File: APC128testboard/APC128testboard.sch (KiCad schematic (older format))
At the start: 75 parts, among them P1 MAXV_CONNB, P10 SPYPAD, P11 SPYPAD, P12 SPYPAD, P13 SPYPAD, P14 SPYPAD, P15 SPYPAD, P16 SPYPAD, P17 SPYPAD, P18 BNC, P19 SPYPAD, P2 MAXV_CONNA, P20 SPYPAD, P21 SPYPAD, P22 SPYPAD, P23 SPYPAD, P24 SPYPAD, P25 SPYPAD, P26 SPYPAD, P3 SPYPAD, P4 SPYPAD, P5 SPYPAD, P6 SPYPAD, P7 SPYPAD, P8 SPYPAD, P9 SPYPAD, SW1 SWITCH_INV, SW2 SWITCH_INV, SW3 SWITCH_INV, SW4 SWITCH_INV, SW5 SWITCH_INV, U1 APC128, U2 AD8129, U3 AD8129, U4 AD5334

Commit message: single library integrated into project settings.
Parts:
- removed P18: BNC, symbol BNC
- removed SW1, SW2, SW3, SW4: SWITCH_INV, symbol SWITCH_INV
- added JP? (x4): JUMPER3, symbol JUMPER3
- added P?: AMP_PWR, symbol CONN_2
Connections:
- wire segments 182 -> 215
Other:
- note removed: "To Oscilloscope"
- moved on the sheet: P20, P21, P22, P23

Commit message: Update to second proposed design of APC128Testboard
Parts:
- removed P1: MAXV_CONNB, symbol CONN_20X2
- removed P?: AMP_PWR, symbol CONN_2
- removed R10, R12, R14, R16, R18, R20, R22, R24, R26, R28: 300, symbol R
- removed R11, R13, R15, R17, R19, R21, R23, R25, R27: 43, symbol R
- removed R29, R30, R31, R32: R, symbol R
- removed SW5: SWITCH_INV, symbol SWITCH_INV
- added C6, C7: 1uF, symbol C
- added C? (x4): .1uF, symbol C
- added C? (x4): 10uF, symbol C
- added JP1, JP2, JP7: JUMPER3, symbol JUMPER3
- added K1: AMP_PWR, symbol CONN_3
- added K2: LEMO+, symbol LEMO2
- added K3: LEMO-, symbol LEMO2
- added P1, P18, P27, P28, P29, P30: SPYPAD, symbol SPYPAD
- added RP1, RP3: 43, symbol R_PACK8
- added RP2, RP4: 300, symbol R_PACK8
- added U5: MAX1719, MODULE, symbol MAX1719
- R1: value 43 -> RG
- R2: value 300 -> RF
- R3: value 43 -> 50
- R4: value 300 -> RG
- R5: value 43 -> RF
- R6: value 300 -> 50
- R7: value 43 -> R
- R8: value 300 -> 0
- R9: value 43 -> 0
- gave numbers to parts that had none: 4
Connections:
- net labels added: -5V, Out+, Out-, Vamp+, Vamp-
- wire segments 215 -> 232
- no-connect marks 5 -> 19
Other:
- note added: "-5V Voltage Regulator"
- note added: "Amp Voltage Source Selector"
- note added: "Fast amplifiers"
- note added: "POTs for setting some \nanalog levels"
- note added: "Select Pot or DAC as \nanalog sources for APC"
- note added: "To scope"
- note removed: "Fast amplifiers. Not sure if this is correct configuration."
- note removed: "Select Pot or DAC as \nanalog source"
- moved on the sheet: C1, JP3, JP4, JP5, JP6, P17, R33, R34, RV3, RV4, U1, U2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

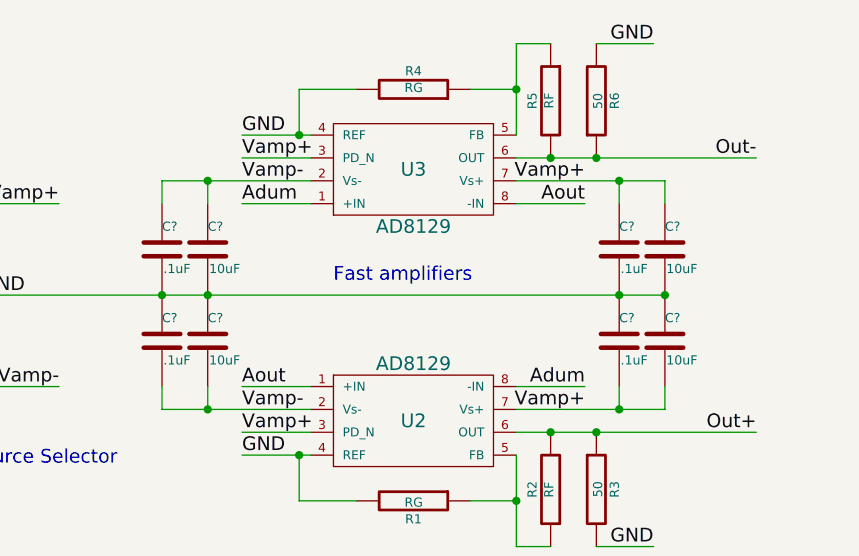
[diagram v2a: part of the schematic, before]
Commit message: Annotated parts on schematic.
Created some missing footprints.
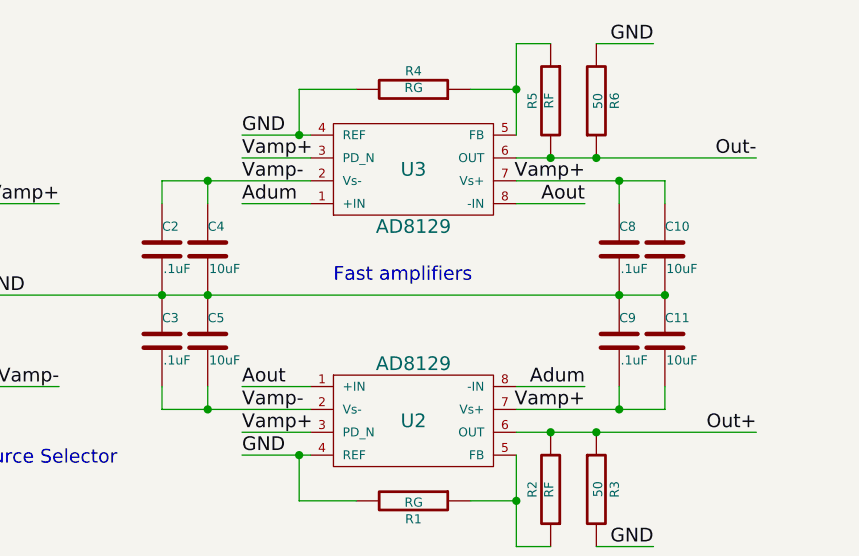
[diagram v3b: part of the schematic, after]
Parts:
- gave numbers to parts that had none: 8
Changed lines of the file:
@@
 Connection ~ 10500 2400
 $Comp
-L C C?
+L C C8
 U 1 1 53944CF9
 P 3950 1500
-F 0 "C?" H 3950 1600 40  0000 L CNN
+F 0 "C8" H 3950 1600 40  0000 L CNN
 F 1 ".1uF" H 3956 1415 40  0000 L CNN
 F 2 "" H 3988 1350 30  0000 C CNN
@@
 $EndComp
 $Comp
-L C C?
+L C C10
 U 1 1 53944CFF
 P 4150 1500
-F 0 "C?" H 4150 1600 40  0000 L CNN
+F 0 "C10" H 4150 1600 40  0000 L CNN
 F 1 "10uF" H 4156 1415 40  0000 L CNN
 F 2 "" H 4188 1350 30  0000 C CNN
@@
 $EndComp
 $Comp
-L C C?
+L C C2
 U 1 1 5394558C
 P 1950 1500
-F 0 "C?" H 1950 1600 40  0000 L CNN
+F 0 "C2" H 1950 1600 40  0000 L CNN
 F 1 ".1uF" H 1956 1415 40  0000 L CNN
 F 2 "" H 1988 1350 30  0000 C CNN
@@
 $EndComp
 $Comp
-L C C?
+L C C4
 U 1 1 53945592
 P 2150 1500
-F 0 "C?" H 2150 1600 40  0000 L CNN
+F 0 "C4" H 2150 1600 40  0000 L CNN
 F 1 "10uF" H 2156 1415 40  0000 L CNN
 F 2 "" H 2188 1350 30  0000 C CNN
@@
 Connection ~ 2150 1200
 $Comp
-L C C?
+L C C3
 U 1 1 53945E78
 P 1950 1900
-F 0 "C?" H 1950 2000 40  0000 L CNN
+F 0 "C3" H 1950 2000 40  0000 L CNN
 F 1 ".1uF" H 1956 1815 40  0000 L CNN
 F 2 "" H 1988 1750 30  0000 C CNN
@@
 $EndComp
 $Comp
-L C C?
+L C C5
 U 1 1 53945E7E
 P 2150 1900
-F 0 "C?" H 2150 2000 40  0000 L CNN
+F 0 "C5" H 2150 2000 40  0000 L CNN
 F 1 "10uF" H 2156 1815 40  0000 L CNN
 F 2 "" H 2188 1750 30  0000 C CNN
@@
 $EndComp
 $Comp
-L C C?
+L C C9
 U 1 1 53945FA2
 P 3950 1900
-F 0 "C?" H 3950 2000 40  0000 L CNN
+F 0 "C9" H 3950 2000 40  0000 L CNN
 F 1 ".1uF" H 3956 1815 40  0000 L CNN
 F 2 "" H 3988 1750 30  0000 C CNN
@@
 $EndComp
 $Comp
-L C C?
+L C C11
 U 1 1 53945FA8
 P 4150 1900
-F 0 "C?" H 4150 2000 40  0000 L CNN
+F 0 "C11" H 4150 2000 40  0000 L CNN
 F 1 "10uF" H 4156 1815 40  0000 L CNN
 F 2 "" H 4188 1750 30  0000 C CNN

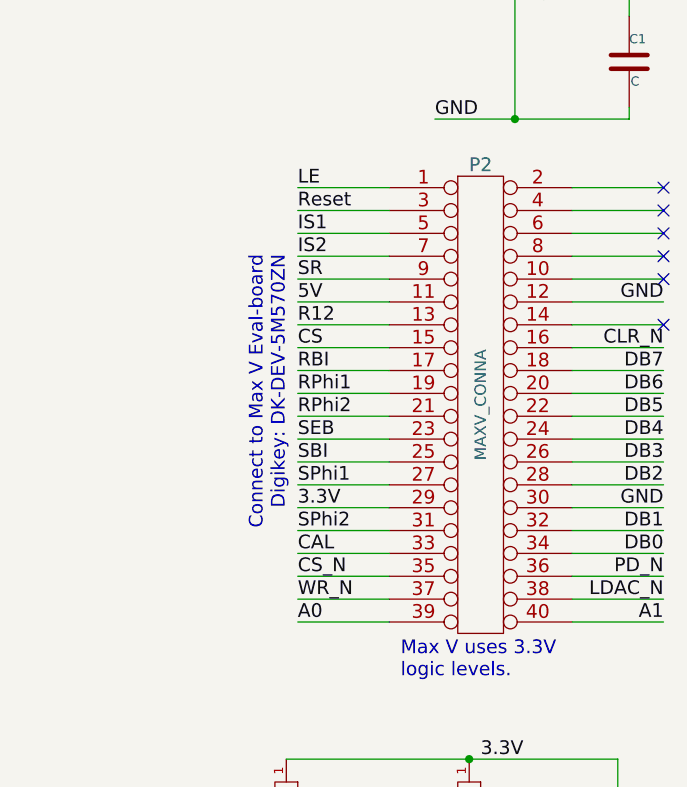
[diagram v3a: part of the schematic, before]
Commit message: Began laying out PCB for APC128testboard.
modified parallel pinout for APC128testboard schematic
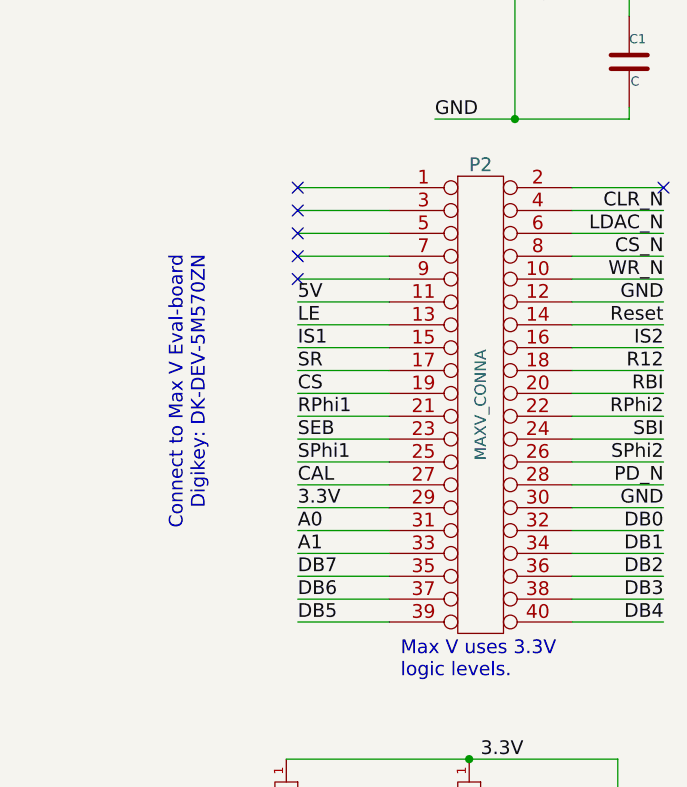
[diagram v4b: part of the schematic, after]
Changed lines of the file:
@@
 Text Label 7100 4850 1    60   ~ 0
 SPhi2_d
-Text Label 9550 2700 0    60   ~ 0
+Text Label 9550 3300 0    60   ~ 0
 LE
-Text Label 9550 2800 0    60   ~ 0
+Text Label 11150 3300 2    60   ~ 0
 Reset
-Text Label 9550 2900 0    60   ~ 0
+Text Label 9550 3400 0    60   ~ 0
 IS1
-Text Label 9550 3000 0    60   ~ 0
+Text Label 11150 3400 2    60   ~ 0
 IS2
-Text Label 9550 3100 0    60   ~ 0
+Text Label 9550 3500 0    60   ~ 0
 SR
-Text Label 9550 3300 0    60   ~ 0
+Text Label 11150 3500 2    60   ~ 0
 R12
-Text Label 9550 3400 0    60   ~ 0
+Text Label 9550 3600 0    60   ~ 0
 CS
-Text Label 9550 3500 0    60   ~ 0
+Text Label 11150 3600 2    60   ~ 0
 RBI
-Text Label 9550 3600 0    60   ~ 0
+Text Label 9550 3700 0    60   ~ 0
 RPhi1
-Text Label 9550 3700 0    60   ~ 0
+Text Label 11150 3700 2    60   ~ 0
 RPhi2
 Text Label 9550 3800 0    60   ~ 0
 SEB
+Text Label 11150 3800 2    60   ~ 0
+SBI
 Text Label 9550 3900 0    60   ~ 0
-SBI
-Text Label 9550 4000 0    60   ~ 0
 SPhi1
-Text Label 9550 4200 0    60   ~ 0
+Text Label 11150 3900 2    60   ~ 0
 SPhi2
 $Comp
@@
 Text Label 4500 4850 1    60   ~ 0
 VANA
-Text Label 9550 4300 0    60   ~ 0
+Text Label 9550 4000 0    60   ~ 0
 CAL
-Text Label 9550 4400 0    60   ~ 0
+Text Label 11150 3000 2    60   ~ 0
 CS_N
 Text Label 6000 4850 1    60   ~ 0
 RBO
+Text Label 11150 3100 2    60   ~ 0
+WR_N
+Text Label 9550 4200 0    60   ~ 0
+A0
+Text Label 9550 4300 0    60   ~ 0
+A1
+Text Label 11150 2900 2    60   ~ 0
+LDAC_N
+Text Label 11150 4000 2    60   ~ 0
+PD_N
+Text Label 11150 4200 2    60   ~ 0
+DB0
+Text Label 11150 4300 2    60   ~ 0
+DB1
+Text Label 11150 4400 2    60   ~ 0
+DB2
+Text Label 11150 4500 2    60   ~ 0
+DB3
+Text Label 11150 4600 2    60   ~ 0
+DB4
+Text Label 9550 4600 0    60   ~ 0
+DB5
 Text Label 9550 4500 0    60   ~ 0
-WR_N
-Text Label 9550 4600 0    60   ~ 0
-A0
-Text Label 11150 4600 2    60   ~ 0
-A1
-Text Label 11150 4500 2    60   ~ 0
-LDAC_N
-Text Label 11150 4400 2    60   ~ 0
-PD_N
-Text Label 11150 4300 2    60   ~ 0
-DB0
-Text Label 11150 4200 2    60   ~ 0
-DB1
-Text Label 11150 4000 2    60   ~ 0
-DB2
-Text Label 11150 3900 2    60   ~ 0
-DB3
-Text Label 11150 3800 2    60   ~ 0
-DB4
-Text Label 11150 3700 2    60   ~ 0
-DB5
-Text Label 11150 3600 2    60   ~ 0
 DB6
-Text Label 11150 3500 2    60   ~ 0
+Text Label 9550 4400 0    60   ~ 0
 DB7
-Text Label 11150 3400 2    60   ~ 0
+Text Label 11150 2800 2    60   ~ 0
 CLR_N
 $Comp
@@
 Text Notes 10000 4850 0    60   ~ 0
 Max V uses 3.3V\nlogic levels.
-Text Notes 9500 3000 3    60   ~ 0
+Text Notes 9150 3000 3    60   ~ 0
 Connect to Max V Eval-board\nDigikey: DK-DEV-5M570ZN
 Text Notes 1200 3950 0    60   ~ 0
@@
 	-1   0    0    1
 $EndComp
-NoConn ~ 11150 2700
-NoConn ~ 11150 2800
-NoConn ~ 11150 2900
-NoConn ~ 11150 3000
-NoConn ~ 11150 3100
 $Comp
 L SPYPAD P29
@@
 Connection ~ 4150 1700
 Connection ~ 3950 1700
-NoConn ~ 11150 3300
+NoConn ~ 9550 2700
+NoConn ~ 9550 2800
+NoConn ~ 9550 2900
+NoConn ~ 9550 3000
+NoConn ~ 9550 3100
+NoConn ~ 11150 2700
 $EndSCHEMATC

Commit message: Update V0.3. First iteration on PCB  for APC128Testboard complete.
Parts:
- removed P16, P19, P20, P22, P23, P24, P25, P26, P27: SPYPAD, symbol SPYPAD
- added J1: CONN-SCSI68, symbol CONN-SCSI68
- added R10, R12: 0, symbol R
- added R11: ?, symbol R
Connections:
- net labels added: DTB_IO0, DTB_IO1, DTB_IO2, DTB_IO3
- net labels removed: Out+, Out-
- wire segments 232 -> 252
- no-connect marks 19 -> 13
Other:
- note added: "To DTB"
- note removed: "To scope"
- moved on the sheet: K2, P18, P21, P29, R7, R8, U1

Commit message: Fourth proposal for APC128 Testboard.
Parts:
- removed C10, C11: 10uF, symbol C
- removed C8, C9: .1uF, symbol C
- removed R2, R5: RF, symbol R
- removed R3: 50, symbol R
- removed R4: RG, symbol R
- removed U2, U3: AD8129, symbol AD8129
- added P16: SPYPAD, symbol SPYPAD
- added U2: AD8131, symbol AD8131
- R1: value RG -> 50
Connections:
- net labels added: +OUT, -OUT, DTB_OUT+, DTB_OUT-
- net labels removed: OUT+, OUT-
- wire segments 252 -> 257
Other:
- note added: "Fast amplifier\nGain: x2"
- note added: "Out to Scope"
- note removed: "Fast amplifiers"
- moved on the sheet: C2, C4, K2, K3, P29, P30, R6, R8, R9

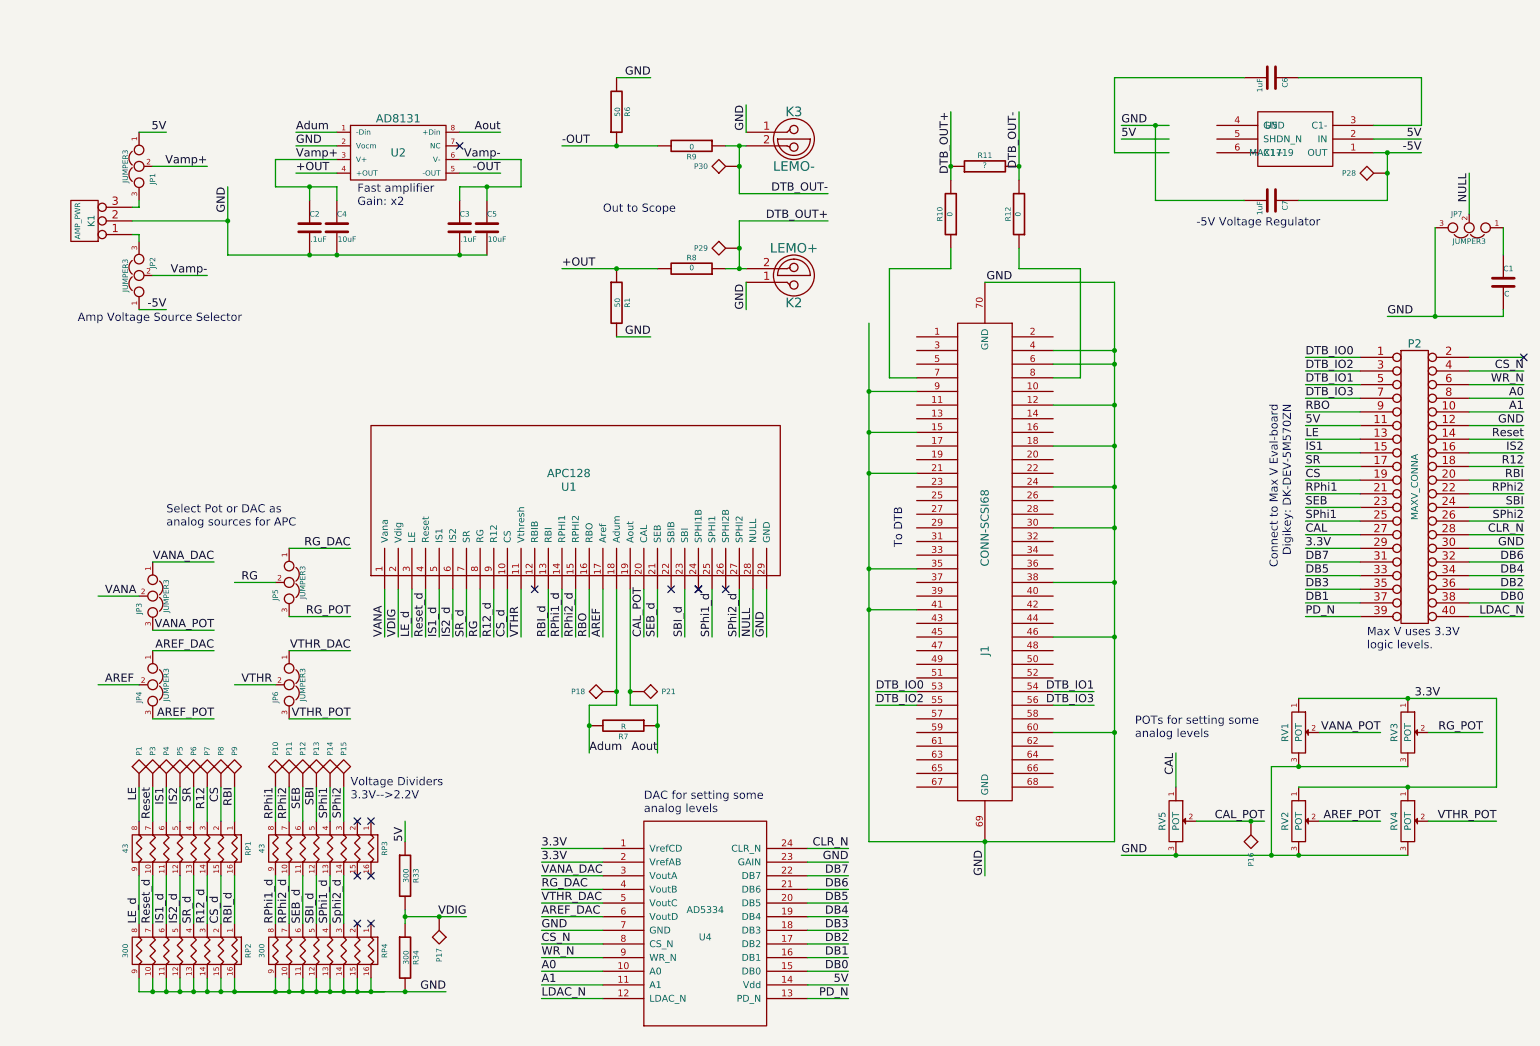
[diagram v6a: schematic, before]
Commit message: Update to version 4 of APC128Testboard. Added external 5V supply and 3.3V Regulator.
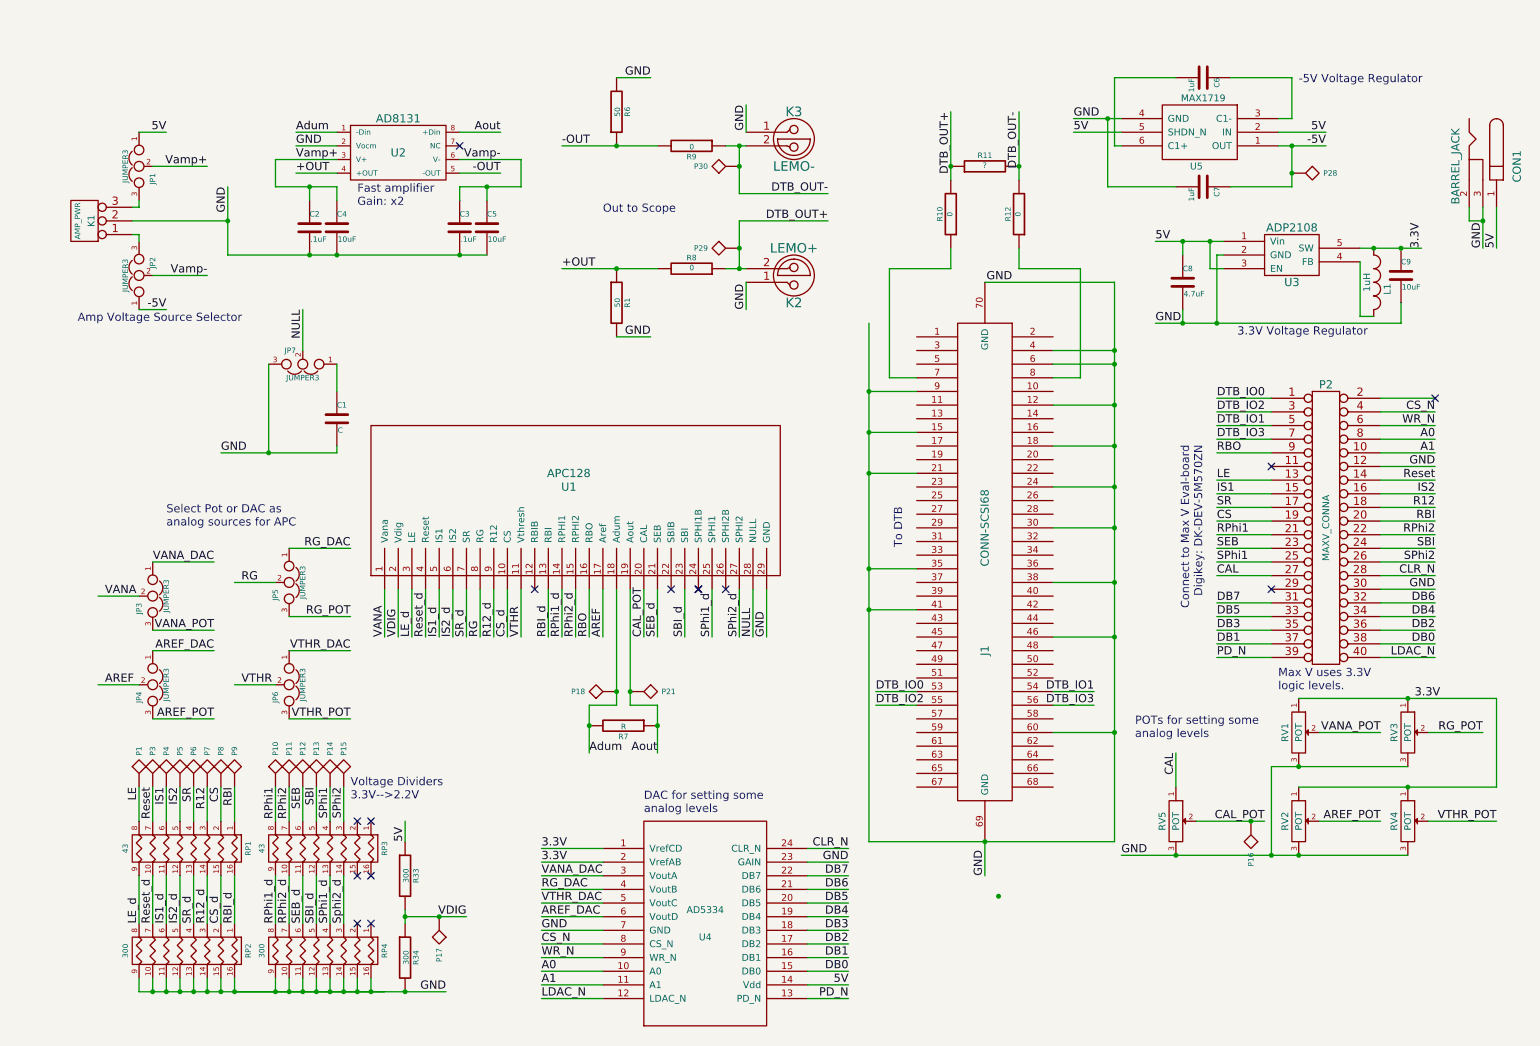
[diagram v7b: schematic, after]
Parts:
- added C8: 4.7uF, symbol C
- added C9: 10uF, symbol C
- added CON1: BARREL_JACK, symbol BARREL_JACK
- added L1: 1uH, symbol INDUCTOR_SMALL
- added U3: ADP2108, symbol ADP2108
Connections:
- wire segments 257 -> 271
- no-connect marks 13 -> 15
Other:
- note added: "3.3V Voltage Regulator"
- moved on the sheet: C1, C6, C7, JP7, P2, P28, U5
